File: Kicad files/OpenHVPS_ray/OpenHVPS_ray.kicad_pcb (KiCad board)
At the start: 2 copper layers, 40.6 x 20.8 mm, 70 parts, among them J2 Conn_01x03_Male, Q1 FQT7N10, Q2 BC846A, Q3 MMDT3906, U1 MAX6008AEUR+T, U2 74HC14, U3 MAX4162, U4 CD14538BM

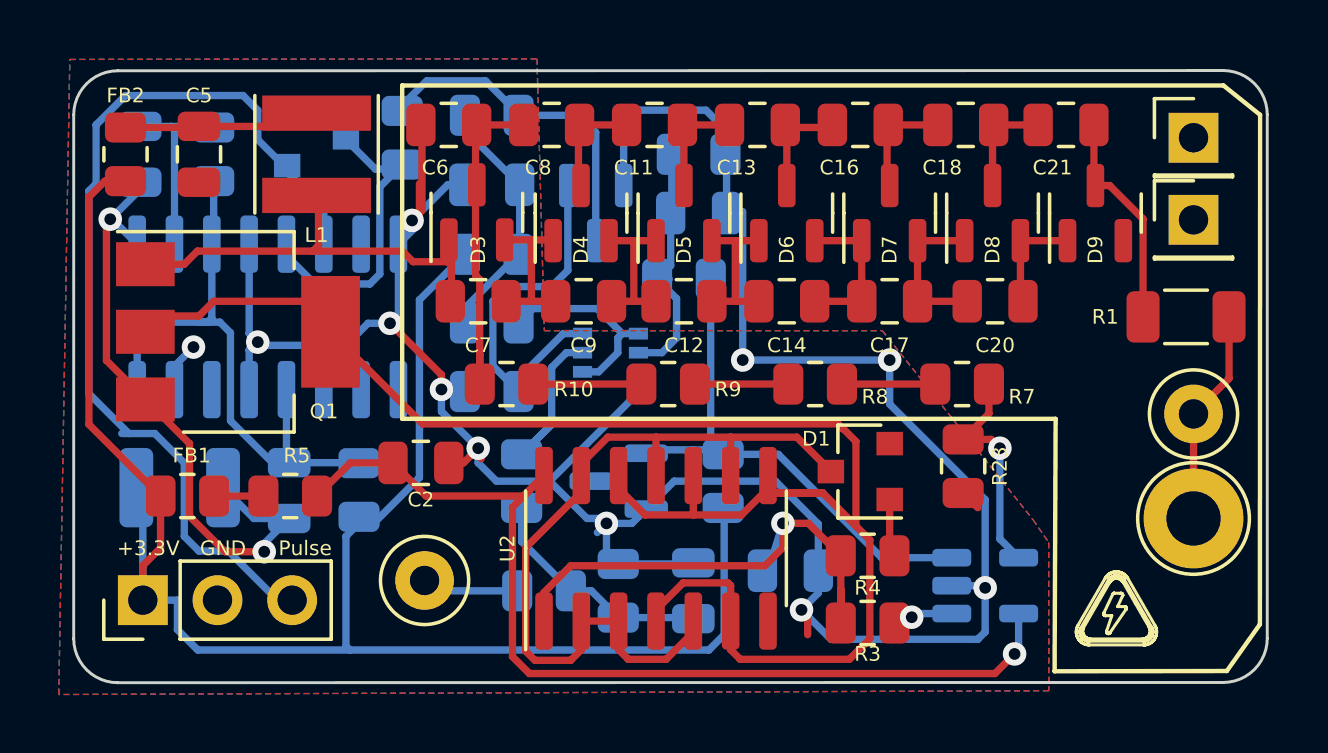
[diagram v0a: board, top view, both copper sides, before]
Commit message: fixed a couple of errors in BOM. reduced size of 2 diodes
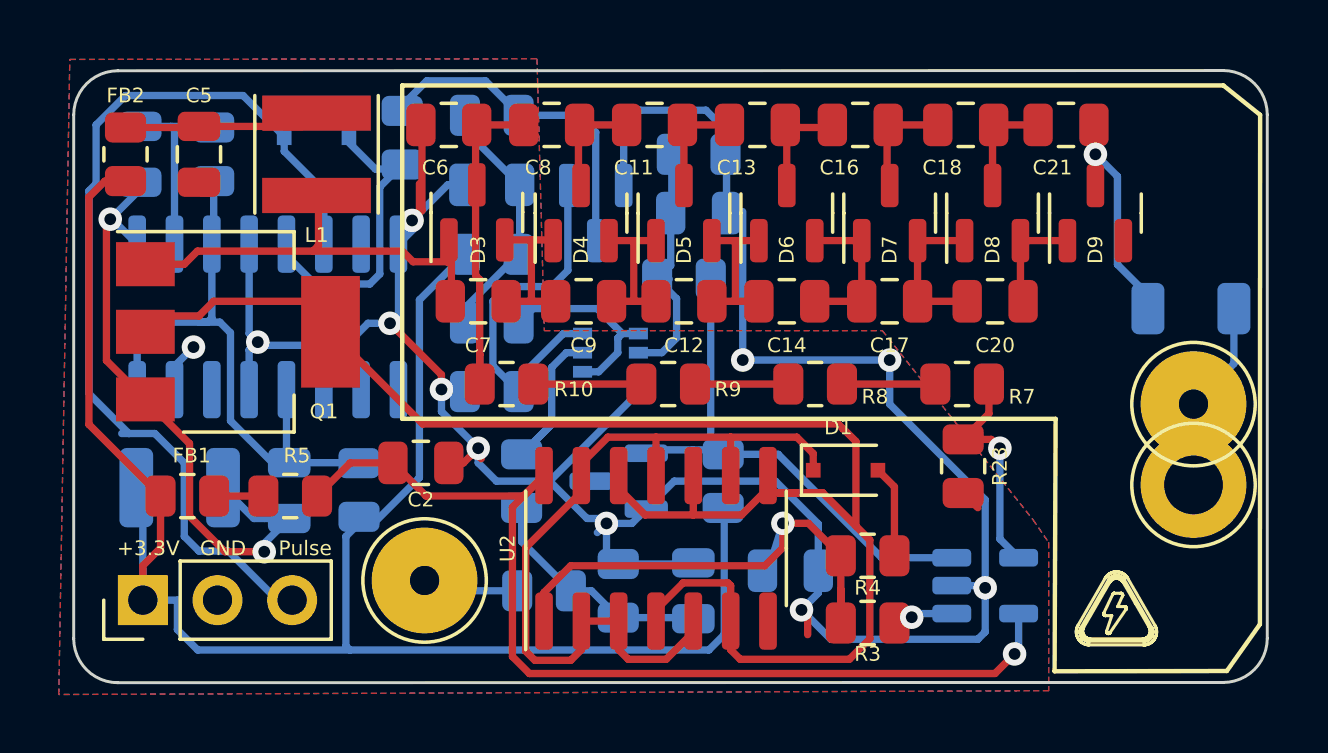
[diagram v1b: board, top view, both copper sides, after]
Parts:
- removed ?: LOGO, Symbol:QR_code_SafePulse
- removed REF** (x2): PinHeader_1x01_P2.54mm_Vertical, Connector_PinHeader_2.54mm:PinHeader_1x01_P2.54mm_Vertical
- D1, D2: value BAS16 -> BAS16J; footprint Diode_SMD:D_SOT-23_ANK -> Diode_SMD:D_SOD-323F
- H1, H2: footprint TestPoint:TestPoint_Loop_D2.50mm_Drill1.0mm -> TestPoint:TestPoint_Loop_D3.80mm_Drill2.0mm
- H2: footprint TestPoint:TestPoint_Loop_D2.50mm_Drill1.85mm -> TestPoint:TestPoint_Loop_D3.80mm_Drill2.0mm
- R1: moved to B.Cu
- moved H2 1.14 mm to (164.3, 71.2)
- moved D1 0.50 mm to (152.5, 70.8), turned to 0 degrees
- moved H2 0.33 mm to (164.3, 68.5)
- moved R1 0.33 mm to (164.2, 65.2)
- turned D2 to 180 degrees
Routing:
- net Net-(D1-Pad2): track 1.75 -> 3.14 mm
- net Net-(C21-Pad2): track 7.63 -> 7.74 mm, vias 0 -> 1
